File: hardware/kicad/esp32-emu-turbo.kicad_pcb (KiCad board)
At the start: 4 copper layers, 160 x 75 mm, 71 parts, among them J1 USB-C-16P, J3 JST-PH-2P, J4 FPC-40P-0.5mm, SW1 SW-SMD-5.1x5.1, SW10 SW-SMD-5.1x5.1, SW11 SW-SMD-5.1x5.1, SW12 SW-SMD-5.1x5.1, SW13 SW-SMD-5.1x5.1, SW2 SW-SMD-5.1x5.1, SW3 SW-SMD-5.1x5.1, SW4 SW-SMD-5.1x5.1, SW5 SW-SMD-5.1x5.1, SW6 SW-SMD-5.1x5.1, SW7 SW-SMD-5.1x5.1, SW8 SW-SMD-5.1x5.1, SW9 SW-SMD-5.1x5.1, U1 ESP32-S3-WROOM-1-N16R8, U2 ESOP-8, U3 SOT-223, U5 SOP-16, U6 TF-01A

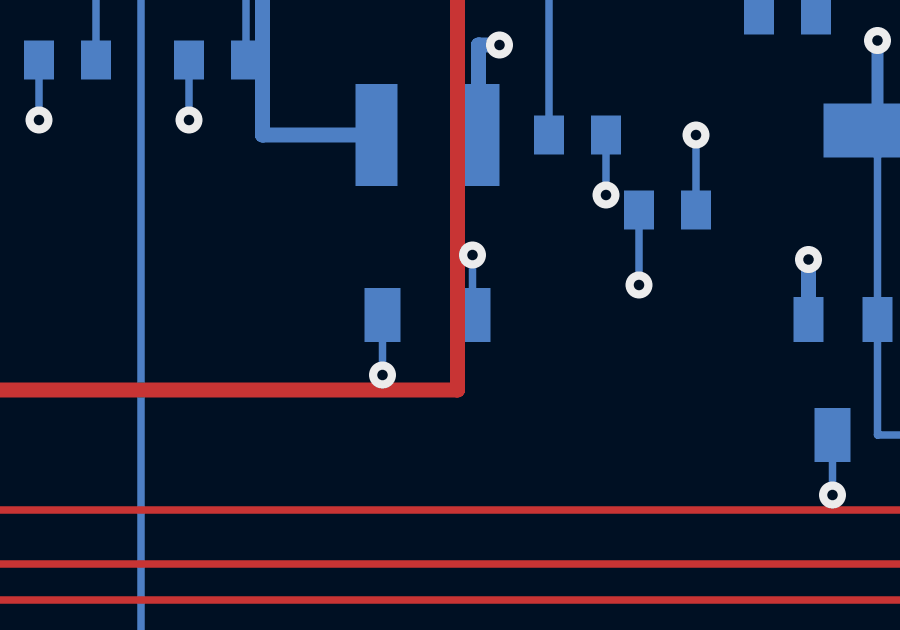
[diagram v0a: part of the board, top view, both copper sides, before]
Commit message: fix(pcb): resolve C19 via-to-VBUS power short on F.Cu
C19 vias overlapped VBUS traces on F.Cu causing all power rails to short
to GND on all 5 assembled boards. GND via at (108.5, 60.5) overlapped
VBUS horizontal @y=61 by -0.20mm; +5V via at (111.5, 56.5) overlapped
VBUS vertical @x=111 by -0.20mm. Fix moves GND via to y=59.5 (gap 0.80mm)
and routes +5V via to x=113 (gap 1.30mm). Includes incident documentation
and rework guide for existing boards.

Co-Authored-By: Claude Opus 4.6 (1M context) <noreply@anthropic.com>
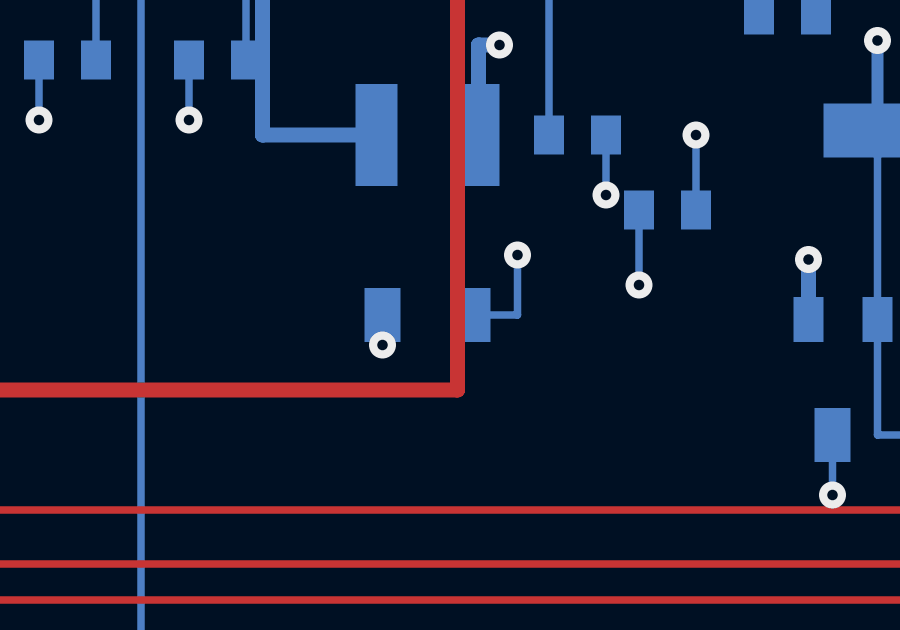
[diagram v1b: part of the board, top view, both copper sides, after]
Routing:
- net +5V: track 25.2 -> 26.7 mm
- net GND: track 107.8 -> 106.8 mm
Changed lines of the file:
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@@
   (segment (start 117.05 55.0) (end 117.05 57.5) (width 0.25) (layer "B.Cu") (net 1))
   (via (at 117.05 57.5) (size 0.9) (drill 0.35) (layers "F.Cu" "B.Cu") (net 1))
-  (segment (start 111.5 58.5) (end 111.5 56.5) (width 0.25) (layer "B.Cu") (net 3))
-  (via (at 111.5 56.5) (size 0.9) (drill 0.35) (layers "F.Cu" "B.Cu") (net 3))
-  (segment (start 108.5 58.5) (end 108.5 60.5) (width 0.25) (layer "B.Cu") (net 1))
-  (via (at 108.5 60.5) (size 0.9) (drill 0.35) (layers "F.Cu" "B.Cu") (net 1))
+  (segment (start 111.5 58.5) (end 113.0 58.5) (width 0.25) (layer "B.Cu") (net 3))
+  (segment (start 113.0 58.5) (end 113.0 56.5) (width 0.25) (layer "B.Cu") (net 3))
+  (via (at 113.0 56.5) (size 0.9) (drill 0.35) (layers "F.Cu" "B.Cu") (net 3))
+  (segment (start 108.5 58.5) (end 108.5 59.5) (width 0.25) (layer "B.Cu") (net 1))
+  (via (at 108.5 59.5) (size 0.9) (drill 0.35) (layers "F.Cu" "B.Cu") (net 1))
   (via (at 25.95 63.0) (size 0.9) (drill 0.35) (layers "F.Cu" "B.Cu") (net 4))
   (segment (start 25.95 63.0) (end 25.95 65.0) (width 0.25) (layer "B.Cu") (net 4))

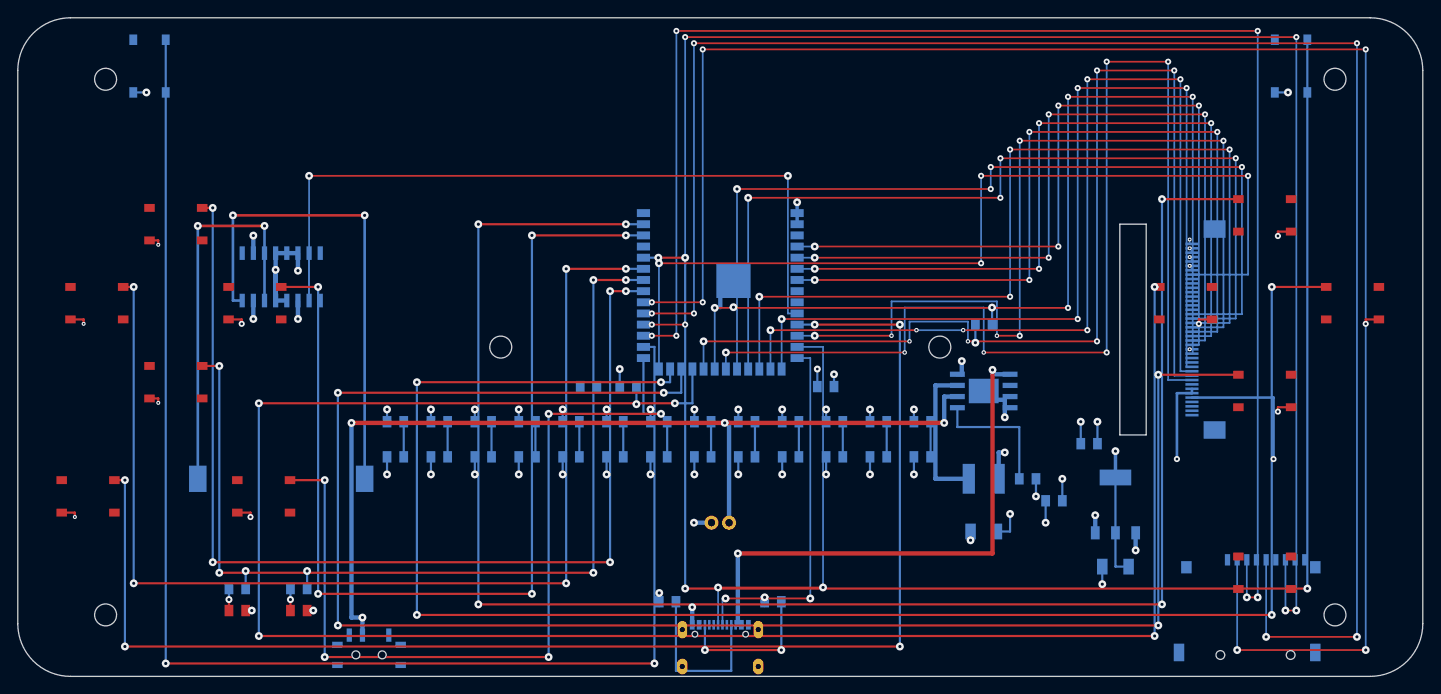
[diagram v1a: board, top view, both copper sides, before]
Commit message: fix(pcb): eliminate all 13 collision suppressions (13 → 0)
Reroute button approach columns to resolve all clearance violations:

- BTN_A/X/Y: reduce vias 0.46→0.35mm, widen gap 0.42→0.50mm
- BTN_L: move approach x=72.50→68.00, F.Cu stub to ESP32 pad
- BTN_R: F.Cu L-shape jog x=76.20→65.00, bypass U1:23/SD_MISO/BTN_Y
- BTN_Y GND: route via RIGHT(x=140) then DOWN(y=49), avoid LCD/BTN_X

Collision grid: 0 violations, 0 suppressed (was 13 suppressed)
DFM v2: 88/88 pass | DFA: 9/9 pass

Co-Authored-By: Claude Opus 4.6 (1M context) <noreply@anthropic.com>
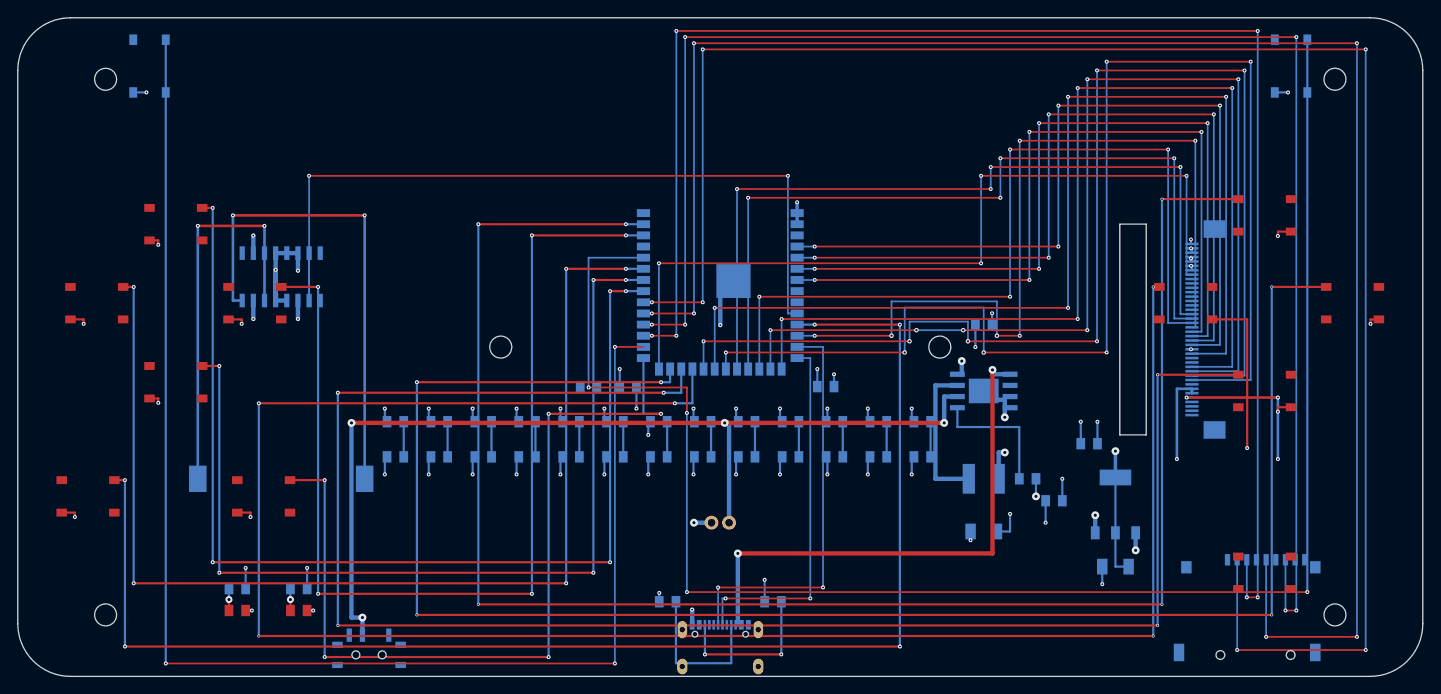
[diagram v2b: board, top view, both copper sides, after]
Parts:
- removed the U3 at (125.0, 55.5)
- added R2: R_0805, R_0805, B.Cu at (86.0, 66.5)
- U3: renamed from R2; value R_0805 -> SOT-223; footprint R_0805 -> SOT-223
- moved U3 40.5 mm to (125.0, 55.5)
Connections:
- U3 pad 1: USB_CC2 -> GND
- U3 pad 2: GND -> (no net)
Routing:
- net GND: track 106.8 -> 131.5 mm, vias 49 -> 51
- net LCD_CS: track 134.6 -> 147.9 mm
- net BTN_R: track 179.8 -> 193.1 mm
- net LCD_BL: track 106.7 -> 93.9 mm
- net LCD_DC: track 128.9 -> 140.8 mm
- net LCD_D7: track 102.9 -> 91.6 mm
- net LCD_WR: track 114.2 -> 124.8 mm
- net LCD_D6: track 102.8 -> 92.8 mm
- net LCD_RD: track 110.5 -> 119.7 mm
- net LCD_D5: track 102.6 -> 94.0 mm
- net LCD_RST: track 114.8 -> 122.4 mm
- net LCD_D4: track 103.4 -> 97.0 mm
- net +3V3: track 53.2 -> 59.6 mm
- net LCD_D0: track 89.8 -> 94.6 mm
- net LCD_D3: track 90.3 -> 86.7 mm
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
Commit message: feat(pcb): add silkscreen labels + brand text "ESP32-EMU-TURBO CPJ & CP"
- Front: "DISPLAY AREA", "D-PAD", "ABXY", "MENU", "CHG", "FULL" on F.SilkS
- Back: "ESP32-S3", "IP5306", "AMS1117", "PAM8403", "USB-C", "SD", "PWR",
  "SPEAKER", "L", "R" on B.SilkS
- Brand: "ESP32-EMU-TURBO CPJ & CP" on F.Fab at Y=73 (below display,
  F.Fab due to J1 shield pads at Y=73.9 blocking SilkS)
- Component refs stay on Fab (SilkS causes silk_over_copper DFM violations)
- DFM: 88/88 pass, 0 silk issues, 0 collision suppressions

Co-Authored-By: Claude Opus 4.6 (1M context) <noreply@anthropic.com>
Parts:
- removed the C3 at (69.5, 42.0)
- removed the C4 at (92.0, 42.0)
- removed the J1 at (80.0, 71.5)
- removed the J3 at (80.0, 57.5)
- removed the L1 at (110.0, 52.5)
- removed the R1 at (74.0, 66.5)
- removed the R18 at (32.0, 65.0)
- removed the R2 at (86.0, 66.5)
- removed the R3 at (65.0, 42.0)
- removed the R4 at (43.0, 46.0)
- removed the R5 at (48.0, 46.0)
- removed the U2 at (110.0, 42.5)
- removed the U5 at (30.0, 29.5)
- added C1: C_0805, C_0805, B.Cu at (122.0, 48.5)
- added C11: C_0805, C_0805, B.Cu at (73.0, 50.0)
- added C12: C_0805, C_0805, B.Cu at (78.0, 50.0)
- added C13: C_0805, C_0805, B.Cu at (83.0, 50.0)
- added C14: C_0805, C_0805, B.Cu at (88.0, 50.0)
- added C15: C_0805, C_0805, B.Cu at (93.0, 50.0)
- added C16: C_0805, C_0805, B.Cu at (98.0, 50.0)
- added C17: C_0805, C_0805, B.Cu at (110.0, 35.0)
- added C18: C_0805, C_0805, B.Cu at (118.0, 55.0)
- added C19: C_1206, C_1206, B.Cu at (110.0, 58.5)
- added C2: C_1206, C_1206, B.Cu at (125.0, 62.5)
- added C20: C_0805, C_0805, B.Cu at (103.0, 50.0)
- added C21: C_0805, C_0805, B.Cu at (38.0, 23.5)
- added C22: C_0805, C_0805, B.Cu at (33.2, 20.0)
- added C23: C_0805, C_0805, B.Cu at (38.0, 29.5)
- added C24: C_0805, C_0805, B.Cu at (29.4, 22.0)
- added C25: C_0805, C_0805, B.Cu at (31.5, 37.5)
- added R15: R_0805, R_0805, B.Cu at (98.0, 46.0)
- added R20: R_0805, R_0805, B.Cu at (38.0, 26.8)
- added R21: R_0805, R_0805, B.Cu at (38.0, 32.2)
- J1: renamed from R17; value R_0805 -> USB-C-16P; footprint R_0805 -> USB-C-16P
- J3: renamed from C13; value C_0805 -> JST-PH-2P; footprint C_0805 -> JST-PH-2P
- L1: renamed from C12; value C_0805 -> SMD-4x4x2; footprint C_0805 -> SMD-4x4x2
- R1: renamed from C14; value C_0805 -> R_0805; footprint C_0805 -> R_0805
- R17: renamed from C18; value C_0805 -> R_0805; footprint C_0805 -> R_0805
- R18: renamed from C19; value C_1206 -> R_0805; footprint C_1206 -> R_0805
- R2: renamed from C15; value C_0805 -> R_0805; footprint C_0805 -> R_0805
- R3: renamed from C16; value C_0805 -> R_0805; footprint C_0805 -> R_0805
- R4: renamed from C1; value C_0805 -> R_0805; footprint C_0805 -> R_0805
- R5: renamed from C2; value C_1206 -> R_0805; footprint C_1206 -> R_0805
- U2: renamed from R15; value R_0805 -> ESOP-8; footprint R_0805 -> ESOP-8
- U5: renamed from C11; value C_0805 -> SOP-16; footprint C_0805 -> SOP-16
- moved R17 93.5 mm to (25.0, 65.0)
- moved R4 79.0 mm to (43.0, 46.0)
- moved R5 78.7 mm to (48.0, 46.0)
- moved R18 78.3 mm to (32.0, 65.0)
- moved J1 55.4 mm to (80.0, 71.5)
- moved U5 47.6 mm to (30.0, 29.5)
- moved C3 34.4 mm to (69.5, 42.0)
- moved R3 34.0 mm to (65.0, 42.0)
- moved L1 32.1 mm to (110.0, 52.5)
- moved R1 21.6 mm to (74.0, 66.5)
- moved C4 19.3 mm to (92.0, 42.0)
- moved R2 17.9 mm to (86.0, 66.5)
- moved U2 12.5 mm to (110.0, 42.5)
- moved J3 8.08 mm to (80.0, 57.5)
- renumbered C20 to C3, C17 to C4
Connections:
- C3 pad 1: (no net) -> +3V3
- C3 pad 2: (no net) -> GND
- C4 pad 1: VBUS -> +3V3
- J1 pad 1: +3V3 -> (no net)
- J1 pad 2: (no net) -> VBUS
- J3 pad 1: (no net) -> BAT+
- J3 pad 2: (no net) -> GND
- L1 pad 1: (no net) -> BAT+
- L1 pad 2: (no net) -> LX
- R1 pad 1: (no net) -> USB_CC1
- R1 pad 2: (no net) -> GND
- R17 pad 1: BAT+ -> +3V3
- R17 pad 2: GND -> (no net)
- R18 pad 1: +5V -> +3V3
- R18 pad 2: GND -> (no net)
- R2 pad 1: (no net) -> USB_CC2
- R2 pad 2: (no net) -> GND
- R4 pad 1: +5V -> (no net)
- R4 pad 2: GND -> (no net)
- R5 pad 1: +3V3 -> (no net)
- R5 pad 2: GND -> (no net)
- U2 pad 1: (no net) -> VBUS
- U5 pad 2: (no net) -> GND
- U6 pad 10: (no net) -> GND
- U6 pad 12: (no net) -> GND
- U6 pad 4: (no net) -> +3V3
- U6 pad 6: (no net) -> GND
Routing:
- net +5V: track 26.7 -> 46.9 mm, vias 7 -> 9
- net GND: track 131.5 -> 139.0 mm, vias 51 -> 60
- net I2S_DOUT: track 90.8 -> 96.7 mm, vias 2 -> 4
- net PAM_VREF: track 0.00 -> 5.25 mm
- net SD_MOSI: track 174.7 -> 178.3 mm
- net +3V3: vias 21 -> 22
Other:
- board text added: "ESP32-EMU-TURBO CPJ & CP"
- board text added: "ESP32-EMU-TURBO CPJ & CP 2026"
- board text removed: "ESP32 EMU Turbo CPJ&CP v1.0"
- board text removed: "ESP32-EMU-TURBO CPJ&CP 2026"

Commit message: feat(pcb): datasheet audit fixes + PAM8403 passives + passive labels
Datasheet-vs-PCB audit of all 20 BOM components found 3 critical issues:

1. SD Card (U6): VCC/GND pins were floating — added via-in-pad to
   connect pin 4 to In2.Cu +3V3 and pin 6 to In1.Cu GND zones.
   MOSI/BTN_B traces detoured to clear new vias.

2. PAM8403 (U5): 7 missing application circuit passives added:
   C22 (0.47uF DC-blocking), R20/R21 (20k bias), C21 (100nF VREF),
   C23/C24/C25 (1uF VDD/PVDD decoupling). All placed ~5mm from IC.

3. USB-C (J1): shield pad width increased to match datasheet
   (front 1.1→1.7mm, rear 1.2→1.4mm).

Also adds:
- Silkscreen labels for all passive components (no overlaps)
- Datasheet audit report (website/docs/datasheet-audit.md)
- Rework guide for existing boards (website/docs/rework-v2.md)
- Updated docs: components.md, manufacturing.md, schematics.md
- v2 audio coprocessor caps renumbered C26/C27 (avoid C21/C22 conflict)
- 0 collisions, 88/88 DFM PASS, 0 silk violations

Co-Authored-By: Claude Opus 4.6 (1M context) <noreply@anthropic.com>
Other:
- board text added: "C1 10uF"
- board text added: "C17 10uF"
- board text added: "C18 10uF"
- board text added: "C19 22uF"
- board text added: "C2 22uF"
- board text added: "C21 100nF"
- board text added: "C22 0.47u"
- board text added: "C23 1uF"
- board text added: "C24 1uF"
- board text added: "C25 1uF"
- board text added: "C3 100nF"
- board text added: "C4 100nF"
- board text added: "C5-C16,C20 100nF"
- board text added: "L1 1uH"
- board text added: "R1 5.1k"
- board text added: "R16 100k"
- board text added: "R17 1k"
- board text added: "R18 1k"
- board text added: "R2 5.1k"
- board text added: "R20 20k"
- board text added: "R21 20k"
- board text added: "R3 10k"
- board text added: "R4-R15,R19 10k"
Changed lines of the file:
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@@
   (gr_text "R" (at 145.0 10.5) (layer "B.SilkS") (effects (font (size 0.8 0.8) (thickness 0.2)) (justify mirror)))
   (gr_text "ESP32-EMU-TURBO  CPJ & CP  2026" (at 80.0 73.0) (layer "B.Fab") (effects (font (size 1.2 1.2) (thickness 0.2)) (justify mirror)))
+  (gr_text "R4-R15,R19  10k" (at 73 43.5) (layer "B.SilkS") (effects (font (size 0.6 0.6) (thickness 0.2)) (justify mirror)))
+  (gr_text "C5-C16,C20  100nF" (at 73 52.5) (layer "B.SilkS") (effects (font (size 0.6 0.6) (thickness 0.2)) (justify mirror)))
+  (gr_text "R1 5.1k" (at 74.0 65.0) (layer "B.SilkS") (effects (font (size 0.5 0.5) (thickness 0.2)) (justify mirror)))
+  (gr_text "R2 5.1k" (at 86.0 65.0) (layer "B.SilkS") (effects (font (size 0.5 0.5) (thickness 0.2)) (justify mirror)))
+  (gr_text "R3 10k" (at 65.0 40.0) (layer "B.SilkS") (effects (font (size 0.5 0.5) (thickness 0.2)) (justify mirror)))
+  (gr_text "C3 100nF" (at 69.5 40.0) (layer "B.SilkS") (effects (font (size 0.5 0.5) (thickness 0.2)) (justify mirror)))
+  (gr_text "C4 100nF" (at 92.0 40.0) (layer "B.SilkS") (effects (font (size 0.5 0.5) (thickness 0.2)) (justify mirror)))
+  (gr_text "R17 1k" (at 25.0 63.0) (layer "B.SilkS") (effects (font (size 0.5 0.5) (thickness 0.2)) (justify mirror)))
+  (gr_text "R18 1k" (at 32.0 63.0) (layer "B.SilkS") (effects (font (size 0.5 0.5) (thickness 0.2)) (justify mirror)))
+  (gr_text "R16 100k" (at 115.0 50.5) (layer "B.SilkS") (effects (font (size 0.5 0.5) (thickness 0.2)) (justify mirror)))
+  (gr_text "C17 10uF" (at 114.5 35.0) (layer "B.SilkS") (effects (font (size 0.5 0.5) (thickness 0.2)) (justify mirror)))
+  (gr_text "C18 10uF" (at 118.0 57.5) (layer "B.SilkS") (effects (font (size 0.5 0.5) (thickness 0.2)) (justify mirror)))
+  (gr_text "C19 22uF" (at 110.0 61.0) (layer "B.SilkS") (effects (font (size 0.5 0.5) (thickness 0.2)) (justify mirror)))
+  (gr_text "C1 10uF" (at 122.0 46.5) (layer "B.SilkS") (effects (font (size 0.5 0.5) (thickness 0.2)) (justify mirror)))
+  (gr_text "C2 22uF" (at 125.0 60.5) (layer "B.SilkS") (effects (font (size 0.5 0.5) (thickness 0.2)) (justify mirror)))
+  (gr_text "L1 1uH" (at 105.5 52.5) (layer "B.SilkS") (effects (font (size 0.5 0.5) (thickness 0.2)) (justify mirror)))
+  (gr_text "C21 100nF" (at 38.0 21.5) (layer "B.SilkS") (effects (font (size 0.5 0.5) (thickness 0.2)) (justify mirror)))
+  (gr_text "C22 0.47u" (at 29.674999999999997 20.0) (layer "B.SilkS") (effects (font (size 0.5 0.5) (thickness 0.2)) (justify mirror)))
+  (gr_text "R20 20k" (at 41.5 26.8) (layer "B.SilkS") (effects (font (size 0.5 0.5) (thickness 0.2)) (justify mirror)))
+  (gr_text "C23 1uF" (at 41.5 29.5) (layer "B.SilkS") (effects (font (size 0.5 0.5) (thickness 0.2)) (justify mirror)))
+  (gr_text "R21 20k" (at 41.5 32.2) (layer "B.SilkS") (effects (font (size 0.5 0.5) (thickness 0.2)) (justify mirror)))
+  (gr_text "C24 1uF" (at 26.365 22.0) (layer "B.SilkS") (effects (font (size 0.5 0.5) (thickness 0.2)) (justify mirror)))
+  (gr_text "C25 1uF" (at 31.5 40.0) (layer "B.SilkS") (effects (font (size 0.5 0.5) (thickness 0.2)) (justify mirror)))
   (footprint "SW-SMD-5.1x5.1" (at 18.0 23.5) (layer "F.Cu")
     (property "Reference" "SW1" (at 0 -3 0) (layer "F.Fab") (effects (font (size 1 1) (thickness 0.2))))
